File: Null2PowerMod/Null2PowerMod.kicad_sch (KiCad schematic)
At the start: 14 parts, among them J1 USB_C_Receptacle_USB2.0, J2 JST 2-PH, U1 MCP73871

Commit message: JSONAPI maybe?
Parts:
- added L?: L, symbol Device:L
- added U2: TPS61090, Package_DFN_QFN:Texas_S-PVQFN-N16_EP2.7x2.7mm_ThermalVias, symbol Regulator_Switching:TPS61090
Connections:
- new net: L?.2, U2.3 (SW), U2.4 (SW)
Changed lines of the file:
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@@
   (junction (at 201.93 31.75) (diameter 0) (color 0 0 0 0)
+  )
+  (junction (at 49.53 135.89) (diameter 0) (color 0 0 0 0)
   )
   (junction (at 196.85 63.5) (diameter 0) (color 0 0 0 0)
@@
     (stroke (width 0) (type default) (color 0 0 0 0))
   )
+  (wire (pts (xy 49.53 138.43) (xy 49.53 135.89))
+    (stroke (width 0) (type default) (color 0 0 0 0))
+  )
   (wire (pts (xy 196.85 63.5) (xy 203.2 63.5))
     (stroke (width 0) (type default) (color 0 0 0 0))
@@
   )
   (wire (pts (xy 254 63.5) (xy 254 66.04))
+    (stroke (width 0) (type default) (color 0 0 0 0))
+  )
+  (wire (pts (xy 49.53 135.89) (xy 46.99 135.89))
     (stroke (width 0) (type default) (color 0 0 0 0))
   )
@@
     (pin "2")
   )
+  (symbol (lib_id "Device:L") (at 43.18 135.89 90) (unit 1)
+    (in_bom yes) (on_board yes) (fields_autoplaced)
+    (property "Reference" "L?" (id 0) (at 43.18 129.54 90))
+    (property "Value" "L" (id 1) (at 43.18 132.08 90))
+    (property "Footprint" "" (id 2) (at 43.18 135.89 0)
+      (effects (font (size 1.27 1.27)) hide)
+    )
+    (property "Datasheet" "~" (id 3) (at 43.18 135.89 0)
+      (effects (font (size 1.27 1.27)) hide)
+    )
+    (pin "1")
+    (pin "2")
+  )
   (symbol (lib_id "power:VBUS") (at 49.53 20.32 0) (unit 1)
     (in_bom yes) (on_board yes) (fields_autoplaced)
@@
     (pin "2")
   )
+  (symbol (lib_id "Regulator_Switching:TPS61090") (at 59.69 148.59 0) (unit 1)
+    (in_bom yes) (on_board yes) (fields_autoplaced)
+    (property "Reference" "U2" (id 0) (at 59.69 129.54 0))
+    (property "Value" "TPS61090" (id 1) (at 59.69 132.08 0))
+    (property "Footprint" "Package_DFN_QFN:Texas_S-PVQFN-N16_EP2.7x2.7mm_ThermalVias" (id 2) (at 35.56 175.26 0)
+      (effects (font (size 1.27 1.27)) (justify left) hide)
+    )
+    (property "Datasheet" "http://www.ti.com/lit/ds/symlink/tps61090.pdf" (id 3) (at 63.5 177.8 0)
+      (effects (font (size 1.27 1.27)) (justify left) hide)
+    )
+    (pin "1")
+    (pin "10")
+    (pin "11")
+    (pin "12")
+    (pin "13")
+    (pin "14")
+    (pin "15")
+    (pin "16")
+    (pin "17")
+    (pin "2")
+    (pin "3")
+    (pin "4")
+    (pin "5")
+    (pin "6")
+    (pin "7")
+    (pin "8")
+    (pin "9")
+  )
   (symbol (lib_id "Device:C") (at 248.92 49.53 0) (unit 1)
     (in_bom yes) (on_board yes) (fields_autoplaced)
@@
       (reference "J2") (unit 1) (value "JST 2-PH") (footprint "Connector_JST:JST_EH_S2B-EH_1x02_P2.50mm_Horizontal")
     )
+    (path "/7f7b0a95-3138-455d-a0bd-13f7fff4ff75"
+      (reference "L?") (unit 1) (value "L") (footprint "")
+    )
     (path "/e3625821-fc01-4ea3-be71-33888b3cdeab"
       (reference "R1") (unit 1) (value "100k") (footprint "")
@@
       (reference "U1") (unit 1) (value "MCP73871") (footprint "Package_DFN_QFN:QFN-20-1EP_4x4mm_P0.5mm_EP2.5x2.5mm")
     )
-  )
+    (path "/f51d2fcb-cab0-48ea-b6a8-c3aca486d8ae"
+      (reference "U2") (unit 1) (value "TPS61090") (footprint "Package_DFN_QFN:Texas_S-PVQFN-N16_EP2.7x2.7mm_ThermalVias")
+    )
+  )

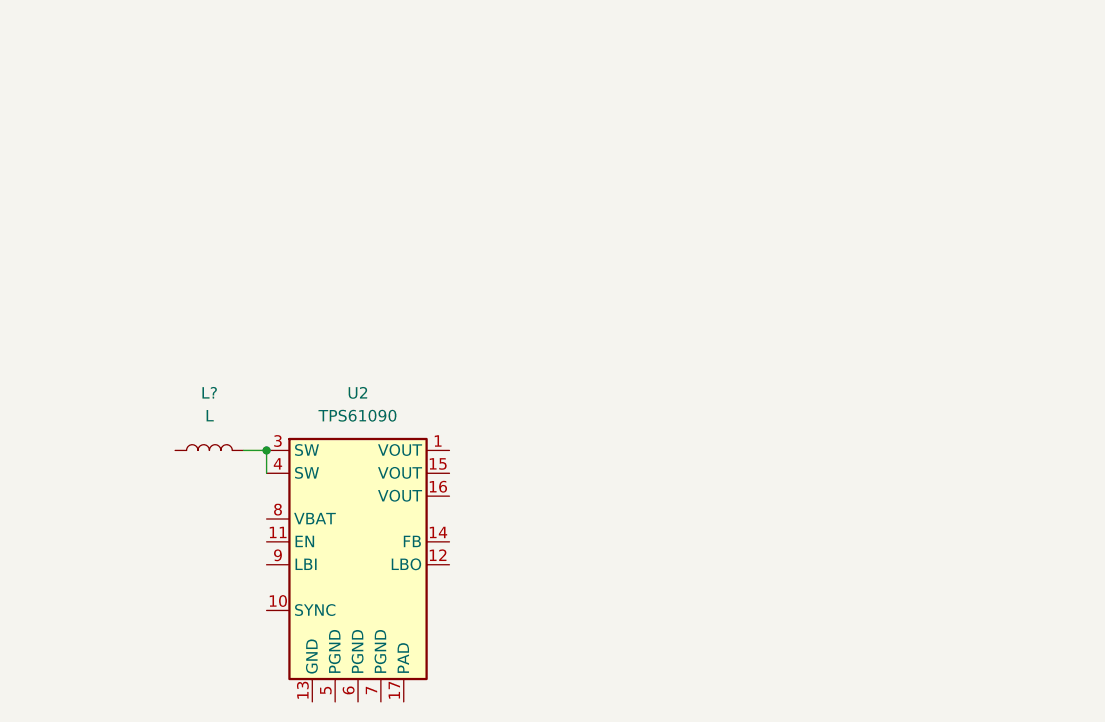
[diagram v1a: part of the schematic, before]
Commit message: Deciding on TPS61030PWP
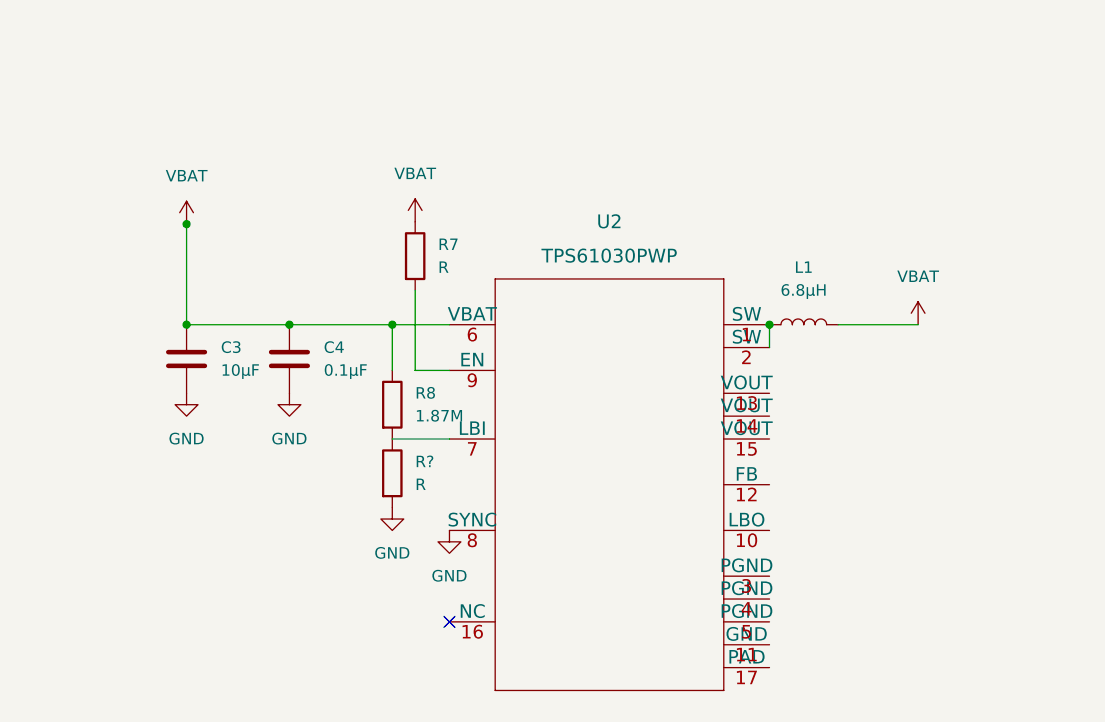
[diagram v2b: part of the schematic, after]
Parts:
- removed L?: L, symbol Device:L
- removed U2: TPS61090, Package_DFN_QFN:Texas_S-PVQFN-N16_EP2.7x2.7mm_ThermalVias, symbol Regulator_Switching:TPS61090
- added C3: 10μF, symbol Device:C
- added C4: 0.1μF, symbol Device:C
- added L1: 6.8μH, symbol Device:L
- added R7, R?: R, symbol Device:R
- added R8: 1.87M, symbol Device:R
- added U2: TPS61030PWP, TPS61030PWP:TPS61030PWP, symbol TPS61030PWP:TPS61030PWP
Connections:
- net GND: now also C3.2, C4.2, R?.2, U2.8 (SYNC)
- net VLIPO: now also C3.1, C4.1, L1.2, R7.1, R8.1, U2.6 (VBAT)
- new net: R7.2, U2.9 (EN)
- new net: L1.1, U2.1 (SW), U2.2 (SW)
- new net: R8.2, R?.1, U2.7 (LBI)
- no-connect marks 10 -> 11

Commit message: expirementing with new tch
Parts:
- added C5: 2.2μF, Capacitor_SMD:C_0201_0603Metric, symbol Device:C
- added C6: 100μF, Capacitor_SMD:C_0201_0603Metric, symbol Device:C_Polarized
- added D3: BLUE, LED_SMD:LED_0201_0603Metric, symbol Device:LED
- added D4: RED, LED_SMD:LED_0201_0603Metric, symbol Device:LED
- added J3: JP2, Connector_PinHeader_1.00mm:PinHeader_1x08_P1.00mm_Vertical, symbol Connector_Generic:Conn_01x08
- added J5, J6: Conn_01x01, Connector_PinHeader_2.54mm:PinHeader_1x01_P2.54mm_Vertical, symbol Connector_Generic:Conn_01x01
- added R10: 1.07MΩ, Resistor_SMD:R_0201_0603Metric, symbol Device:R
- added R11: 200k, Resistor_SMD:R_0201_0603Metric, symbol Device:R
- added R12, R13: 1k, Resistor_SMD:R_0201_0603Metric, symbol Device:R
- added U3: MMUN2133LT1G, MMUN2133LT1G:MMUN2133LT1G, symbol 2022-03-19_03-31-40:MMUN2133LT1G
- C1, C2, C3, C4: footprint (none) -> Capacitor_SMD:C_0201_0603Metric
- D1, D2: footprint (none) -> LED_SMD:LED_0201_0603Metric
- L1: footprint (none) -> Inductor_SMD:L_0201_0603Metric
- R1, R2, R3, R4, R5, R6, R8: footprint (none) -> Resistor_SMD:R_0201_0603Metric
- R7: value R -> 200k; footprint (none) -> Resistor_SMD:R_0201_0603Metric
- R9: renamed from R?; value R -> 340k; footprint (none) -> Resistor_SMD:R_0201_0603Metric
- TH1: footprint (none) -> Libraries:THRMC1005X55N
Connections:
- net GND: now also U2.11 (GND), U2.3 (PGND), U2.4 (PGND), U2.5 (PGND), C5.2, C6.2, D3.1 (K), D4.1 (K), J3.5 (Pin_5), J3.7 (Pin_7), J6.1 (Pin_1), R11.2
- net VLIPO: now also J3.1 (Pin_1), J3.2 (Pin_2), J3.3 (Pin_3), U3.3
- net LB0: now reaches U2.10 (LBO)
- net LB0: now also J3.6 (Pin_6), U3.1
- net at U2.12 (FB): now also R10.2, R11.1
- net +5V: now reaches U2.13 (VOUT)
- net +5V: now also U2.14 (VOUT), U2.15 (VOUT), C5.1, C6.1, J3.8 (Pin_8), J5.1 (Pin_1), R10.1, R12.1
- new net: D3.2 (A), R12.2
- new net: D4.2 (A), R13.2
- new net: R13.1, U3.2
- new net Enable: J3.4 (Pin_4)

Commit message: Feedback changes
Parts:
- C1: value 10μF -> 2.2μF
- C3: value 10μF -> 100μF
- C4: value 0.1μF -> 10μF
- C5: value 2.2μF -> 0.1μF
- C6: value 100μF -> 10μF
- D1: value Orange -> BLUE
- D3: value BLUE -> Orange
- J1: value USB_C_Receptacle_USB2.0 -> Conn_01x01; footprint Connector_USB:USB_C_Receptacle_GCT_USB4085 -> Connector_PinHeader_2.54mm:PinHeader_1x01_P2.54mm_Vertical
- J2: value JST 2-PH -> USB_C_Receptacle_USB2.0; footprint Connector_JST:JST_EH_S2B-EH_1x02_P2.50mm_Horizontal -> Connector_USB:USB_C_Receptacle_GCT_USB4085
- J3: value JP2 -> Conn_01x01; footprint Connector_PinHeader_1.00mm:PinHeader_1x08_P1.00mm_Vertical -> Connector_PinHeader_2.54mm:PinHeader_1x01_P2.54mm_Vertical
- J5: value Conn_01x01 -> JST 2-PH; footprint Connector_PinHeader_2.54mm:PinHeader_1x01_P2.54mm_Vertical -> Connector_JST:JST_EH_S2B-EH_1x02_P2.50mm_Horizontal
- R1: value 100k -> 270k
- R10: value 1.07MΩ -> 340k
- R11: value 200k -> 1.07MΩ
- R13: value 1k -> 1K
- R2: value 100k -> 1k
- R3: value 1k -> 100k
- R4: value 270k -> 200k
- R5: value 1K -> 200k
- R6: value 1K -> 1k
- R7: value 200k -> 1K
- R8: value 1.87M -> 100k
- R9: value 340k -> 1.87M
- U1: value MCP73871 -> MMUN2133LT1G; footprint Package_DFN_QFN:QFN-20-1EP_4x4mm_P0.5mm_EP2.5x2.5mm -> MMUN2133LT1G:MMUN2133LT1G
- U3: value MMUN2133LT1G -> MCP73871; footprint MMUN2133LT1G:MMUN2133LT1G -> Package_DFN_QFN:QFN-20-1EP_4x4mm_P0.5mm_EP2.5x2.5mm

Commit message: implementing feedback
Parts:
- U1: value MMUN2133LT1G -> MCP73871; footprint MMUN2133LT1G:MMUN2133LT1G -> Package_DFN_QFN:QFN-20-1EP_4x4mm_P0.5mm_EP2.5x2.5mm
- U3: value MCP73871 -> MMUN2133LT1G; footprint Package_DFN_QFN:QFN-20-1EP_4x4mm_P0.5mm_EP2.5x2.5mm -> SOT_33LT1G_ONS
